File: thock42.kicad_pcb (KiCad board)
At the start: 2 copper layers, 132 x 102.9 mm, 74 parts, among them J1 OLED-128x32, SW1 SW_PUSH, SW10 SW_PUSH, SW11 SW_PUSH, SW12 SW_PUSH, SW13 SW_PUSH, SW14 SW_PUSH, SW15 SW_PUSH, SW16 SW_PUSH, SW17 SW_PUSH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

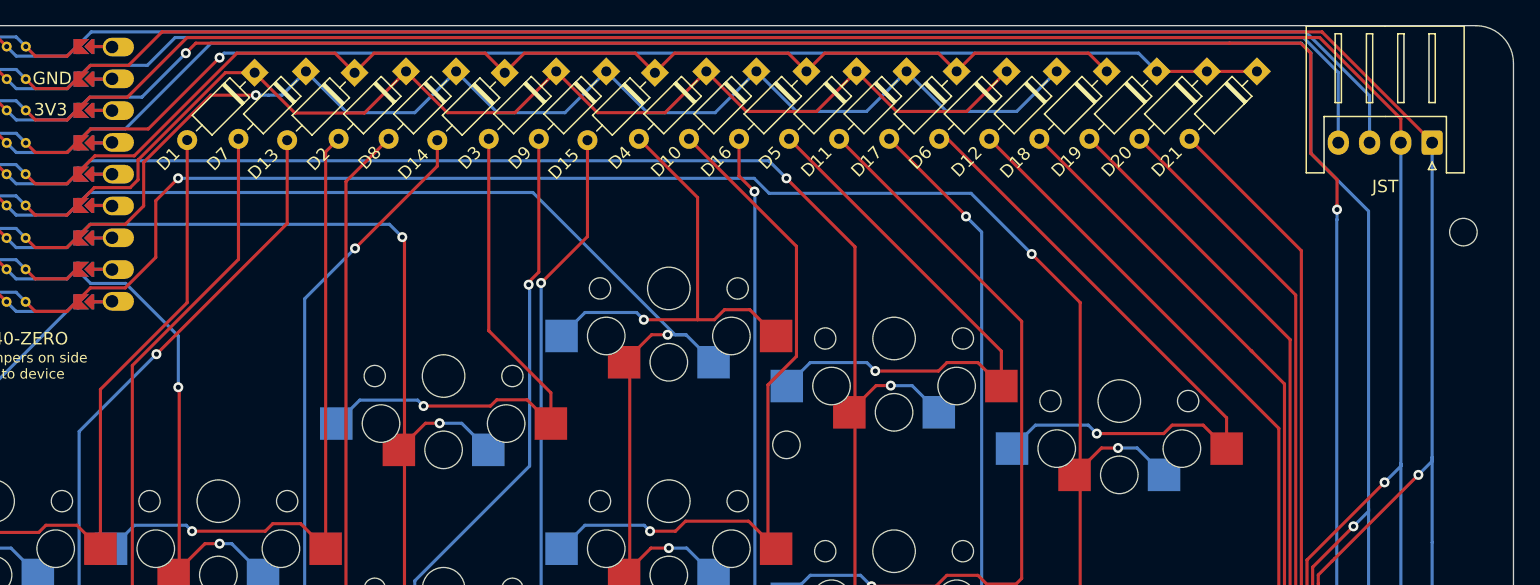
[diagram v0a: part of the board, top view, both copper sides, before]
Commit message: 4pin jst with i2c changed to 3pin jst with serial
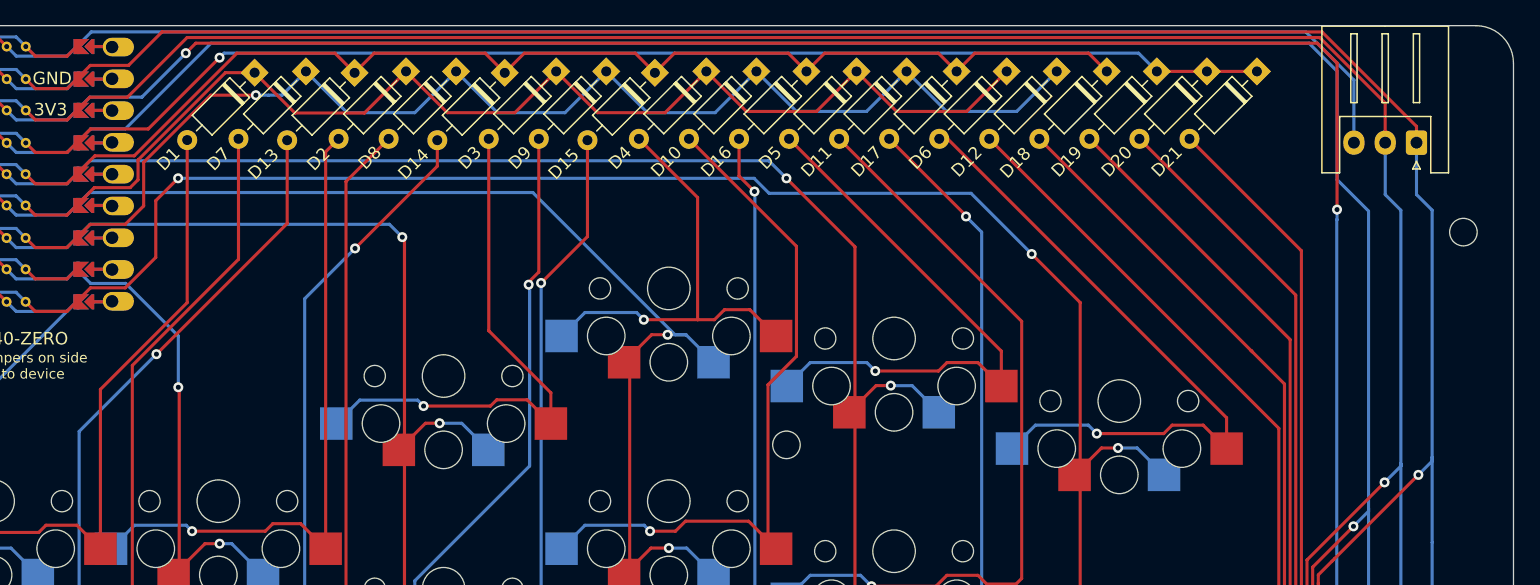
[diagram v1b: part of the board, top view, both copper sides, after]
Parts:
- removed the ? at (211.5, 59.5)
- removed the ? at (212.6, 57.5)
- removed JST: Conn_01x04_Socket, Connector_JST:JST_XH_S4B-XH-A_1x04_P2.50mm_Horizontal
- added ?: , clipboard:99608ffc-c272-47ce-91b9-0f6f16e6904f, B.Cu at (204.1, 59.8)
- added JST_3PIN1: Conn_01x03_Socket, Connector_JST:JST_XH_S3B-XH-A_1x03_P2.50mm_Horizontal, F.Cu at (210.2, 57.4)
- moved ? 1.25 mm to (210.2, 59.5)
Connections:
- U1 pad 1: JST_SDA -> GP0
- U1 pad 2: JST_SDC -> unconnected-(U1-1-Pad2)_3
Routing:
- net JST_SDA: track 109.6 -> 0.00 mm
- net GP0: track 0.00 -> 109.2 mm
- net JST_SDC: track 108.9 -> 0.00 mm
- net OLED_SDA: track 166.0 -> 166.8 mm
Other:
- board text removed: "JST"

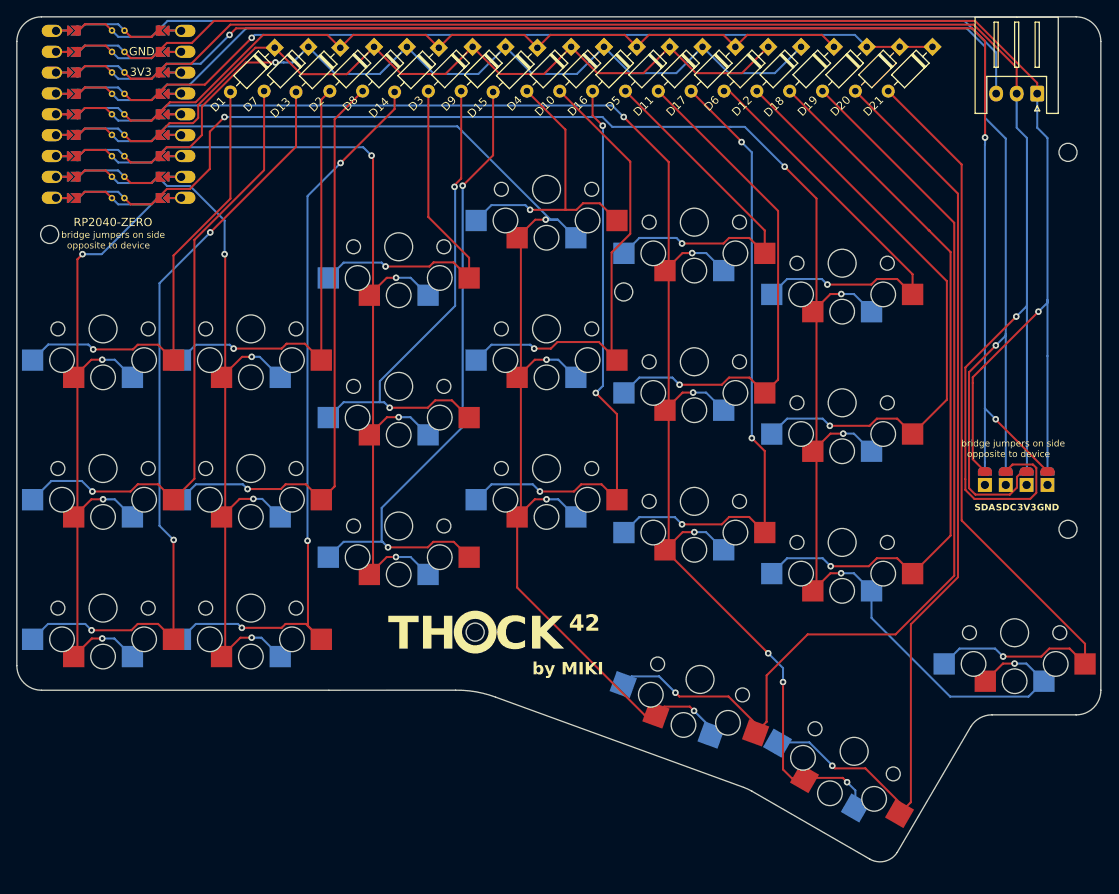
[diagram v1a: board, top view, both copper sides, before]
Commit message: feat: add switch id silkscreen
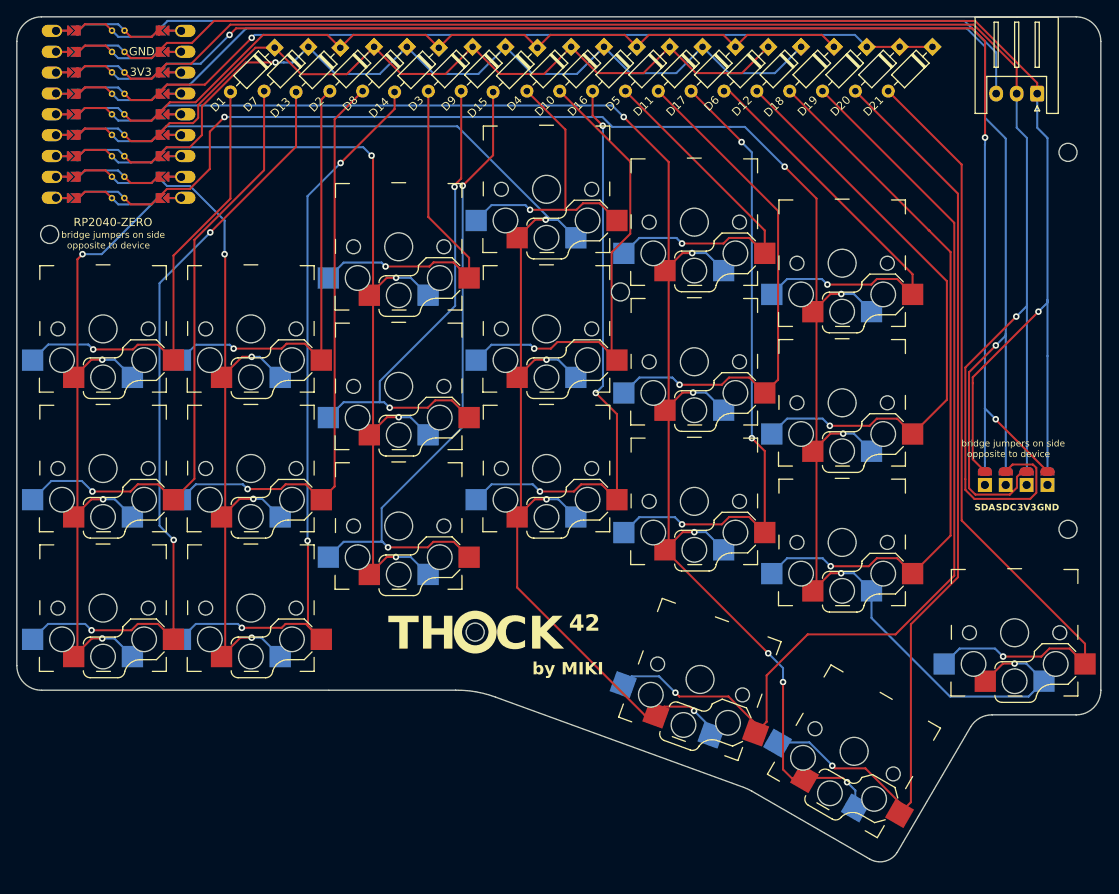
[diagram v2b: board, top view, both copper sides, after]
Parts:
- SW1, SW10, SW11, SW12, SW13, SW14, SW15, SW16, SW17, SW18, SW19, SW2, SW20, SW21, SW3, SW4, SW5, SW6, SW7, SW8, SW9: footprint pg1350:pg1350-RH -> pg1350:pg1350-RH_silkscreen
- moved REF** 0.40 mm to (159.5, 81.5)

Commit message: feat: add more mounting holes
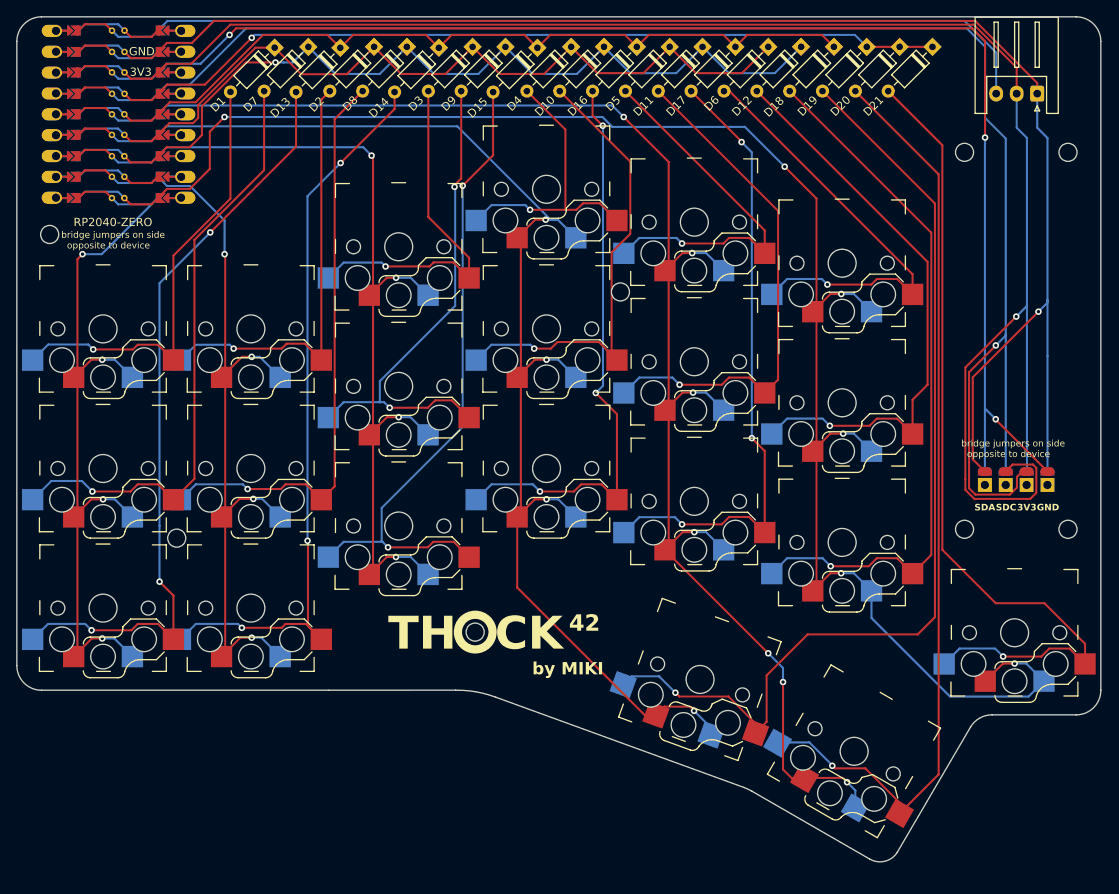
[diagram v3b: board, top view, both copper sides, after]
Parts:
- added REF**: MountingHole_2.2mm_M2, MountingHole:MountingHole_2.2mm_M2, F.Cu at (201.4, 64.5)
- added REF**: MountingHole_2.2mm_M2, MountingHole:MountingHole_2.2mm_M2, F.Cu at (105.5, 111.5)
- added REF**: MountingHole_2.2mm_M2, MountingHole:MountingHole_2.2mm_M2, F.Cu at (201.4, 110.4)
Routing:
- net Net-(D21-A): track 99.2 -> 102.7 mm
- net Net-(D18-A): track 88.5 -> 86.3 mm
- net Net-(D12-A): track 72.5 -> 70.6 mm
- net Net-(D20-A): track 115.4 -> 113.4 mm

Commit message: update links to libs, jst footprint, and add add mounting hole
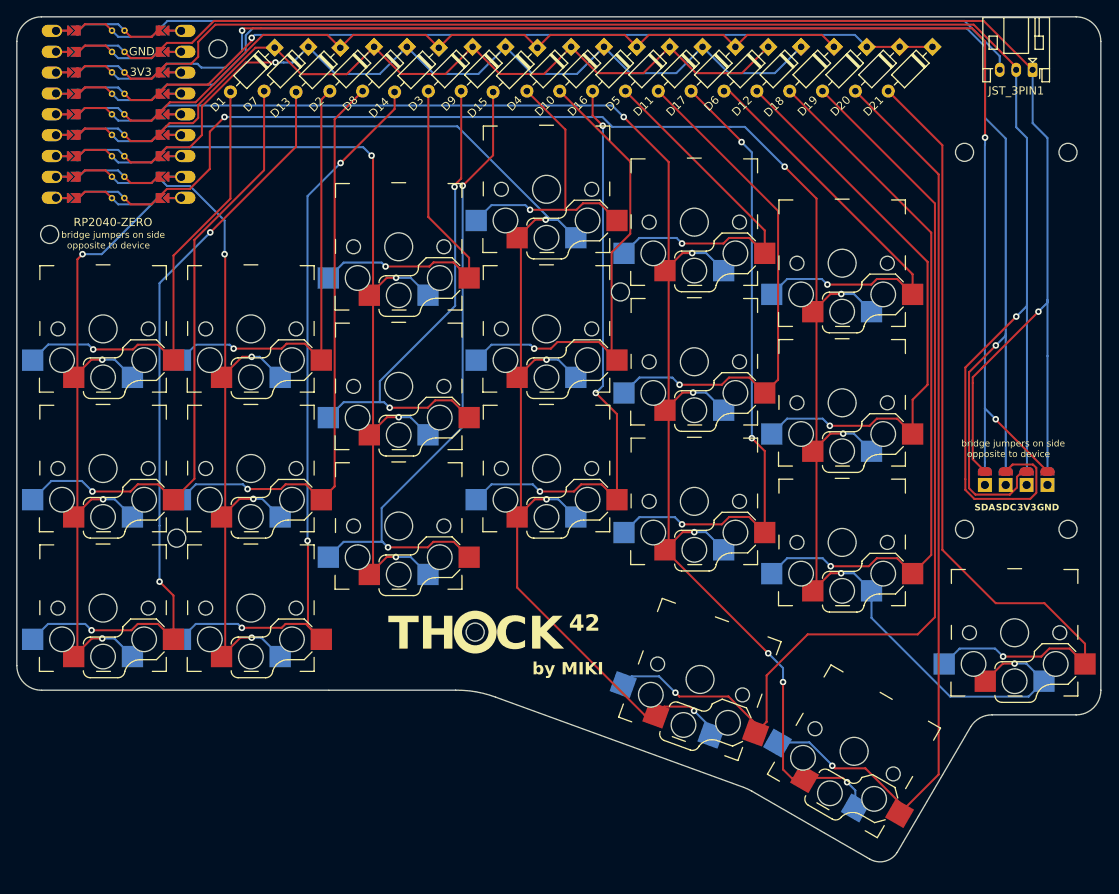
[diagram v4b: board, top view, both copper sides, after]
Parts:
- removed the ? at (210.2, 59.5)
- removed the ? at (204.1, 59.8)
- added ?: , clipboard:093172e0-5c01-45f4-971c-4886d566fe24, B.Cu at (210.6, 54.3)
- added REF**: MountingHole_2.2mm_M2, MountingHole:MountingHole_2.2mm_M2, F.Cu at (110.5, 51.9)
- J1: footprint display_kleeb:OLED-128x32-double-sided -> thock42:OLED-128x32-double-sided
- JST_3PIN1: footprint Connector_JST:JST_XH_S3B-XH-A_1x03_P2.50mm_Horizontal -> Connector_JST:JST_PH_S3B-PH-K_1x03_P2.00mm_Horizontal
- SW1, SW10, SW11, SW12, SW13, SW14, SW15, SW16, SW17, SW18, SW19, SW2, SW20, SW21, SW3, SW4, SW5, SW6, SW7, SW8, SW9: value SW_PUSH -> SW_Push; footprint pg1350:pg1350-RH_silkscreen -> thock42:pg1350-RH_silkscreen
- U1: footprint mcu_kleeb:rp2040-zero-tht_nobtm_reversible -> thock42:rp2040-zero-tht_nobtm_reversible
- moved JST_3PIN1 2.95 mm to (209.7, 54.5)
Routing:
- net GP0: track 109.2 -> 106.4 mm
- net OLED_SDA: track 166.8 -> 168.6 mm
- net OLED_SDC: track 187.6 -> 188.8 mm
- net 3V3: track 201.2 -> 202.3 mm
- net GND: track 184.8 -> 185.4 mm
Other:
- board text added: "JST_3PIN1"

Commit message: add i2c pullups and redesign thumb cluster
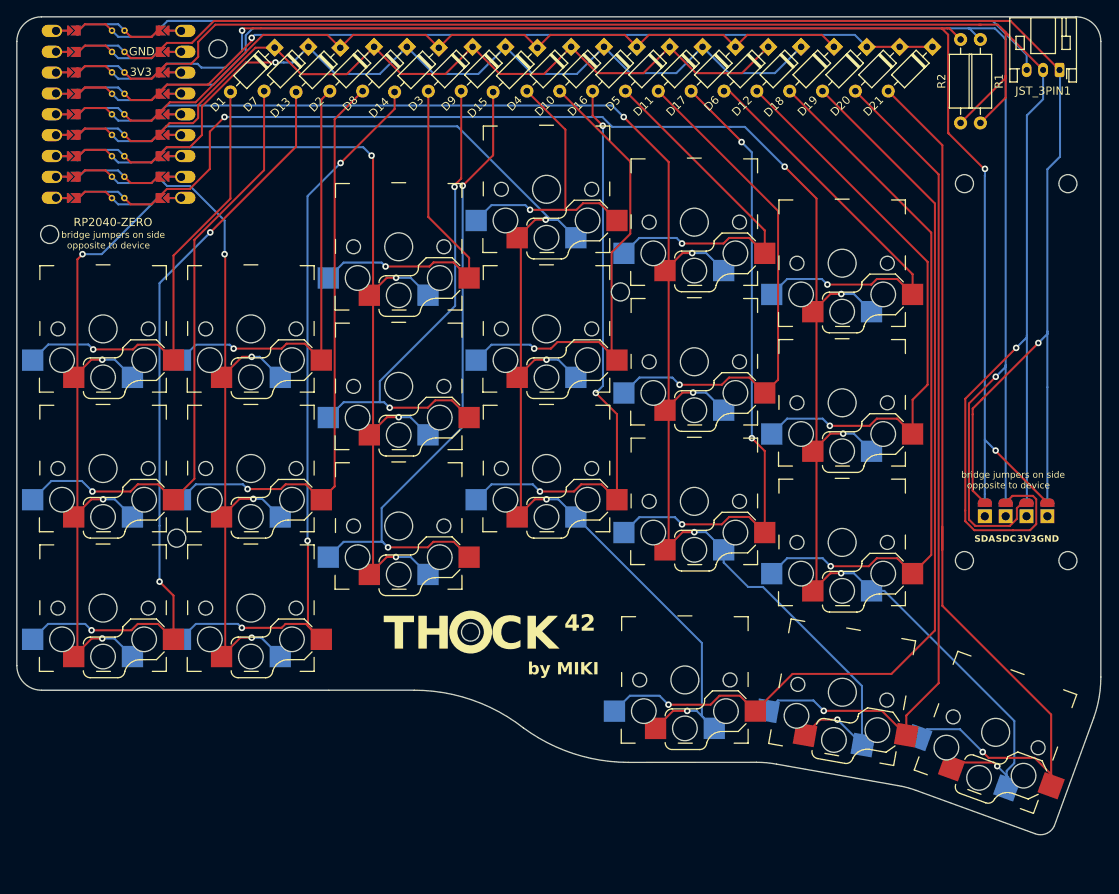
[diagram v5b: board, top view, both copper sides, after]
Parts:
- added R1: R, Resistor_THT:R_Axial_DIN0207_L6.3mm_D2.5mm_P10.16mm_Horizontal, F.Cu at (203.3, 50.8)
- added R2: R, Resistor_THT:R_Axial_DIN0207_L6.3mm_D2.5mm_P10.16mm_Horizontal, F.Cu at (200.9, 50.8)
- moved SW21 12.3 mm to (205.2, 135.1), turned to 160 degrees
- moved SW20 7.33 mm to (186.5, 130.2), turned to 170 degrees
- moved J1 3.81 mm to (201.7, 110.4)
- moved REF** 3.81 mm to (214.0, 114.2)
- moved REF** 3.81 mm to (201.4, 68.3)
- moved REF** 3.81 mm to (214.0, 68.3)
- moved REF** 3.81 mm to (201.4, 114.2)
- moved ? 3.28 mm to (213.8, 54.3)
- moved JST_3PIN1 3.28 mm to (213.0, 54.5)
- moved SW19 1.85 mm to (167.3, 128.7), turned to 180 degrees
- moved REF** 0.56 mm to (141.2, 122.9)
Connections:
- net 3V3 renamed +3V3
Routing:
- net +3V3: track 202.3 -> 231.5 mm
- net Net-(D21-A): track 102.7 -> 115.8 mm
- net Net-(D20-A): track 113.4 -> 103.4 mm
- net OLED_SDC: track 188.8 -> 196.6 mm
- net GND: track 185.4 -> 192.4 mm
- net OLED_SDA: track 168.6 -> 173.3 mm
- net Net-(D19-A): track 120.8 -> 116.9 mm
- net COL5: track 204.5 -> 208.4 mm
- net COL4: track 185.2 -> 181.4 mm, vias 7 -> 5
- net GP0: track 106.4 -> 109.8 mm
- net COL3: track 156.4 -> 157.1 mm
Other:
- board size 132 x 102.9 mm -> 132 x 99.6 mm
